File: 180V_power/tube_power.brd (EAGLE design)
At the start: 50 x 50 mm, 25 parts, among them IC1 NE555D, Q1 IRF740S, Q2 BC546

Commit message: new stuff
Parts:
- removed 7805: 78, iStivi - Transistor-FET-reg:SO08
- removed Q2: BC546, iStivi - Transistor-FET-reg:TO92-EBC
- removed U$1, U$2: (no value), iStivi - Board-Holes:3,2
- removed VR1: 1K, iStivi - RCLD:CA6V
- added R7: 1K, iStivi - RCLD:CA6V
- added U$5, U$6: (no value), iStivi - Board-Holes:3,0
- added U1: TLV1117-5SOT-223, iStivi - Transistor-FET-reg:SOT-223
- added U2: BC817, iStivi - Transistor-FET-reg:SOT-23
- L1: device iStivi - RCLD:TFI0307 -> iStivi - RCLD:RBL0712
- Q1: device iStivi - Transistor-FET:TO263 -> iStivi - Transistor-FET-reg:TO263
- R1: value 56K -> 220K; device iStivi - RCLD:R1206 -> iStivi - RCLD:0207/10
- R2: value 10K -> 470R; device iStivi - RCLD:R1206 -> iStivi - RCLD:0207/10
- R4: value 470R -> 10K; device iStivi - RCLD:0207/10 -> iStivi - RCLD:R1206
- R5: value 220K -> 56K; device iStivi - RCLD:0207/10 -> iStivi - RCLD:R1206
- U$3, U$4: device iStivi - Board-Holes:3,2 -> iStivi - Board-Holes:3,0
- moved C1 33.1 mm to (43.2, 15.2), turned to 0 degrees
- moved R4 26.2 mm to (20.3, 27.9), turned to 180 degrees
- moved Q1 25.4 mm to (34.3, 29.2)
- moved VIN 24.4 mm to (47.0, 24.1), turned to 90 degrees
- moved R5 22.3 mm to (20.3, 22.9), turned to 180 degrees
- moved L1 19.0 mm to (5.08, 14.6), turned to 90 degrees
- moved D1 17.9 mm to (12.7, 13.3), turned to 270 degrees
- moved C4 17.2 mm to (21.0, 12.1), turned to 0 degrees
- moved 180V 16.6 mm to (14.0, 2.54)
- moved C5 16.2 mm to (33.0, 5.71), turned to 0 degrees
- moved IC1 16.2 mm to (21.6, 33.7)
- moved R3 14.5 mm to (20.3, 25.4), turned to 180 degrees
- moved R6 14.5 mm to (20.3, 20.3), turned to 180 degrees
- moved R2 10.6 mm to (15.2, 31.1), turned to 90 degrees
- moved U$4 10.0 mm to (5.00, 35.0)
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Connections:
- net 180V: now also R1.2; no longer R5.2
- net 5V: now also U1.2, U1.4; no longer 7805.2, 7805.3, 7805.6, 7805.7
- net GND: now also R2.1, U1.1, U2.2; no longer 7805.1, Q2.E, R4.1
- net N$10: now also R7.S, U2.1; no longer Q2.B, VR1.S
- net N$26: now also L1.P$2, R5.2, U1.3; no longer 7805.4, L1.2, R1.2
- net N$3: now also R5.1, U2.3; no longer Q2.C, R1.1
- net N$4: now also R4.2; no longer R2.2
- net N$5: now also R4.1; no longer R2.1
- net N$6: now also L1.P$1; no longer L1.1
- net N$8: now also R1.1, R7.E; no longer R5.1, VR1.E
- net N$9: now also R2.2, R7.A; no longer R4.2, VR1.A
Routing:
- net N$1: track 40.9 -> 15.3 mm, vias 2 -> 0
- net GND: track 136.1 -> 113.0 mm
- net N$10: track 33.7 -> 10.9 mm, vias 0 -> 1
- net N$6: track 50.4 -> 69.8 mm, vias 2 -> 1
- net 180V: track 25.2 -> 42.5 mm
- net N$4: track 35.9 -> 18.9 mm
- net N$26: track 116.6 -> 104.3 mm, vias 0 -> 2
- net 5V: track 36.9 -> 24.9 mm, vias 1 -> 0
- net N$5: track 30.9 -> 22.0 mm, vias 4 -> 2
- net N$8: track 4.60 -> 11.1 mm
- net N$3: track 27.7 -> 31.7 mm, vias 1 -> 3
- net N$2: track 7.80 -> 3.81 mm
- net N$9: track 16.6 -> 12.7 mm
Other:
- board size 50 x 50 mm -> 50 x 40 mm
- board text removed: "100uH"
- board text removed: "10uF"
- board text removed: "180V"
- board text removed: "1K"
- board text removed: "2.2uF"
- board text removed: "220K"
- board text removed: "330uF"
- board text removed: "470R"
- board text removed: "5V"
- board text removed: "5V/180V POWER BOARD"
- board text removed: "7805"
- board text removed: "9-12V"
- board text removed: "BC546"
- board text removed: "GND"
- board text removed: "IRF740"
- board text removed: "NE555"
- board text removed: "POWER BOARD"
- board text removed: "Vin"
- board text removed: "iStivi"

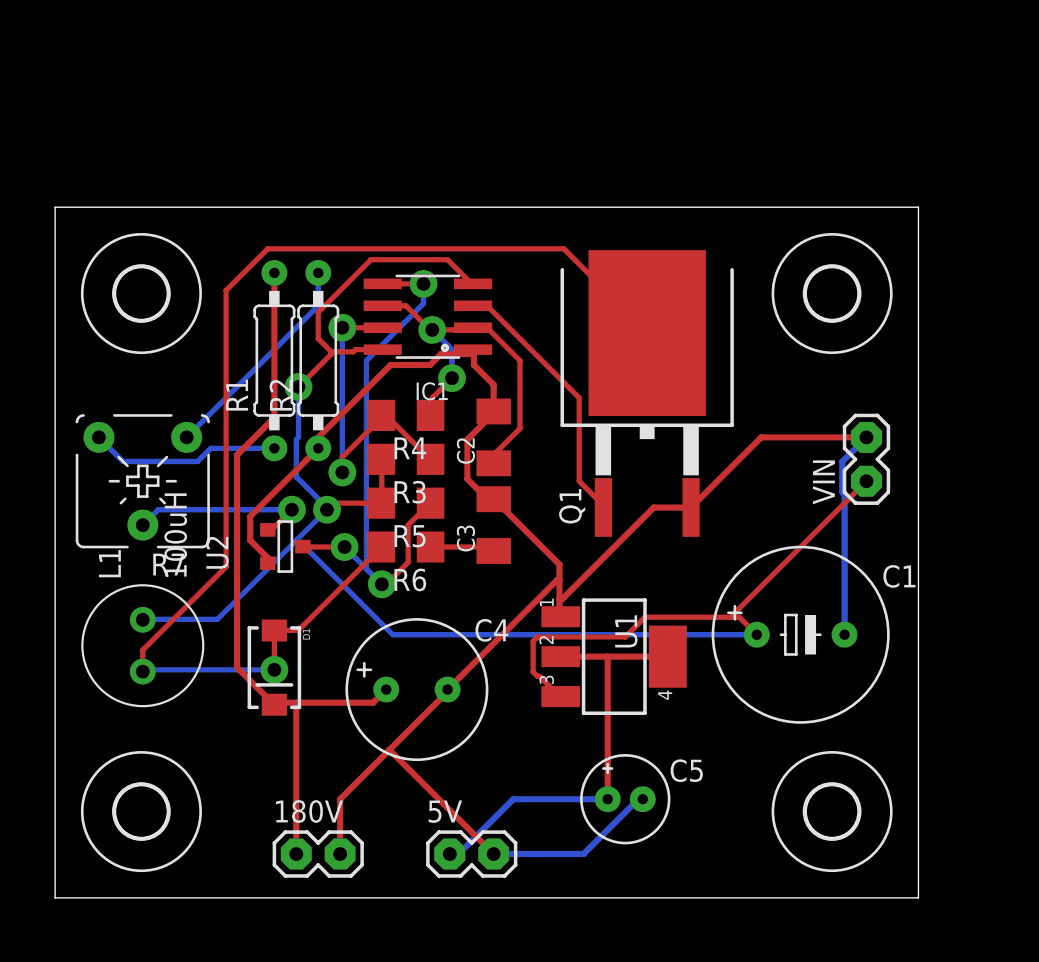
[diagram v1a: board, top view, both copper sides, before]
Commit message: made board smaller for production
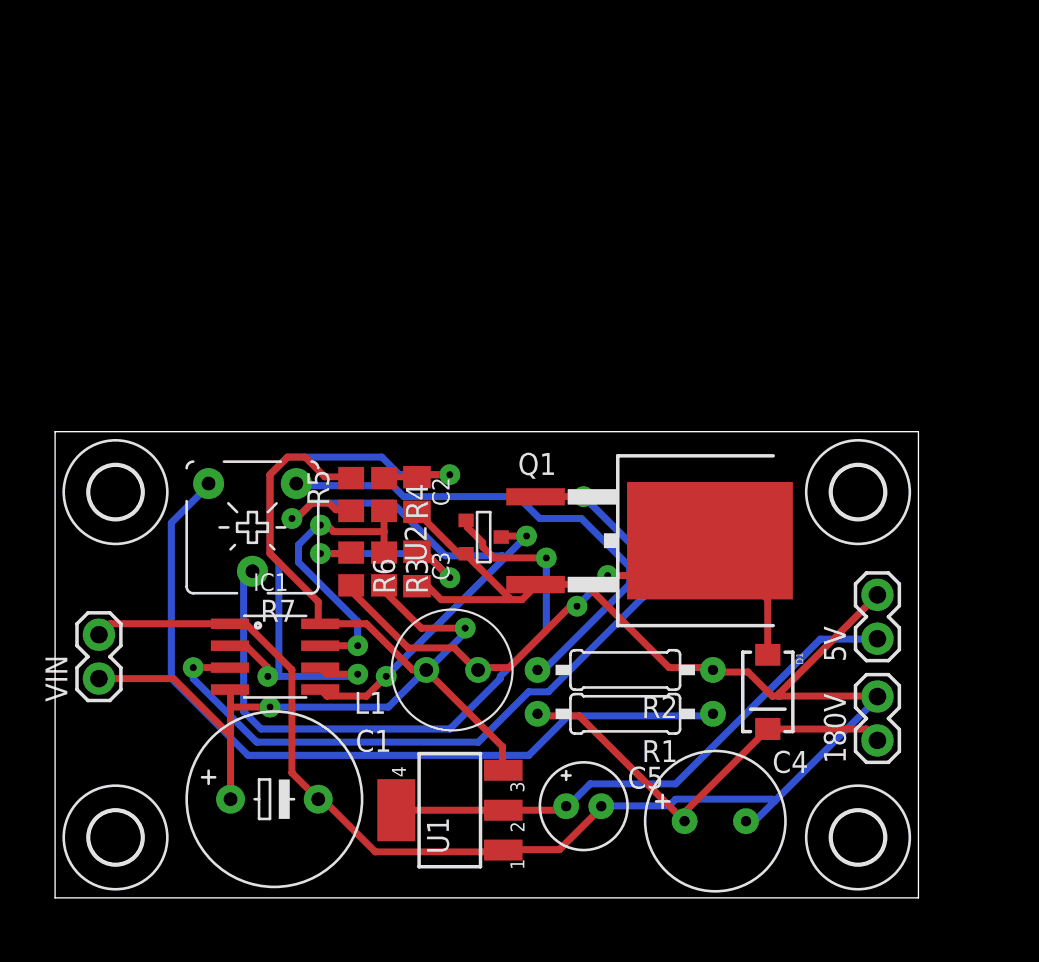
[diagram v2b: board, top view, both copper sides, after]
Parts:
- removed U$3, U$6: (no value), iStivi - Board-Holes:3,0
- added U$1, U$2: (no value), iStivi - Board-Holes:3,0-SMALL
- C2, C3: device iStivi - RCLD:C1206K -> iStivi - RCLD:C0805K
- R3, R4, R5, R6: device iStivi - RCLD:R1206 -> iStivi - RCLD:R0805
- U$4, U$5: device iStivi - Board-Holes:3,0 -> iStivi - Board-Holes:3,0-SMALL
- moved U$4 52.1 mm to (46.5, 3.50)
- moved VIN 45.9 mm to (2.54, 12.7)
- moved 180V 34.3 mm to (47.6, 9.12), turned to 90 degrees
- moved C1 31.9 mm to (12.7, 5.71)
- moved R1 28.8 mm to (33.0, 10.7), turned to 180 degrees
- moved D1 28.6 mm to (41.3, 11.9)
- moved 5V 27.7 mm to (47.6, 15.0), turned to 90 degrees
- moved R2 25.2 mm to (33.0, 13.2), turned to 180 degrees
- moved IC1 21.6 mm to (12.7, 14.0), turned to 270 degrees
- moved C4 18.9 mm to (38.2, 4.45)
- moved L1 18.0 mm to (23.0, 13.2), turned to 180 degrees
- moved U1 13.0 mm to (22.9, 5.08), turned to 90 degrees
- moved U$5 11.6 mm to (46.5, 23.5)
- moved U2 11.5 mm to (24.8, 20.9)
- moved Q1 8.53 mm to (34.4, 20.7), turned to 270 degrees
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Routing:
- net N$26: track 104.3 -> 67.3 mm
- net N$8: track 11.1 -> 46.5 mm
- net N$6: track 69.8 -> 37.6 mm, vias 1 -> 2
- net N$1: track 15.3 -> 43.8 mm, vias 0 -> 2
- net N$10: track 10.9 -> 38.8 mm
- net 180V: track 42.5 -> 25.2 mm
- net N$9: track 12.7 -> 29.8 mm
- net N$5: track 22.0 -> 37.9 mm, vias 2 -> 3
- net N$2: track 3.81 -> 12.5 mm, vias 0 -> 2
- net 5V: track 24.9 -> 32.0 mm
- net GND: track 113.0 -> 106.3 mm
- net N$3: track 31.7 -> 35.5 mm
- net N$4: track 18.9 -> 17.4 mm
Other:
- board size 50 x 40 mm -> 50 x 27 mm

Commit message: board almost final
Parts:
- moved D1 0.63 mm to (41.3, 12.6)
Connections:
- net N$1 renamed OUT
- net N$10 renamed VAR
- net N$2 renamed R6
- net N$26 renamed VCC
- net N$3 renamed CON
- net N$4 renamed DIS
- net N$5 renamed THR
- net N$6 renamed L1
- net N$8 renamed R1
- net N$9 renamed R2
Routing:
- net 180V: track 25.2 -> 26.4 mm
- net OUT: track 43.8 -> 44.9 mm
- net GND: track 106.3 -> 107.0 mm
- net L1: track 37.6 -> 36.9 mm
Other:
- board text added: "100uH"
- board text added: "10uF"
- board text added: "180V"
- board text added: "2.2uF"
- board text added: "220K"
- board text added: "330uF"
- board text added: "470R"
- board text added: "5V"
- board text added: "D1"
- board text added: "GND"
- board text added: "IRF740"
- board text added: "L1"
- board text added: "NE555"
- board text added: "TLV1117"
- board text added: "VIN"
- board text added: "VR1"

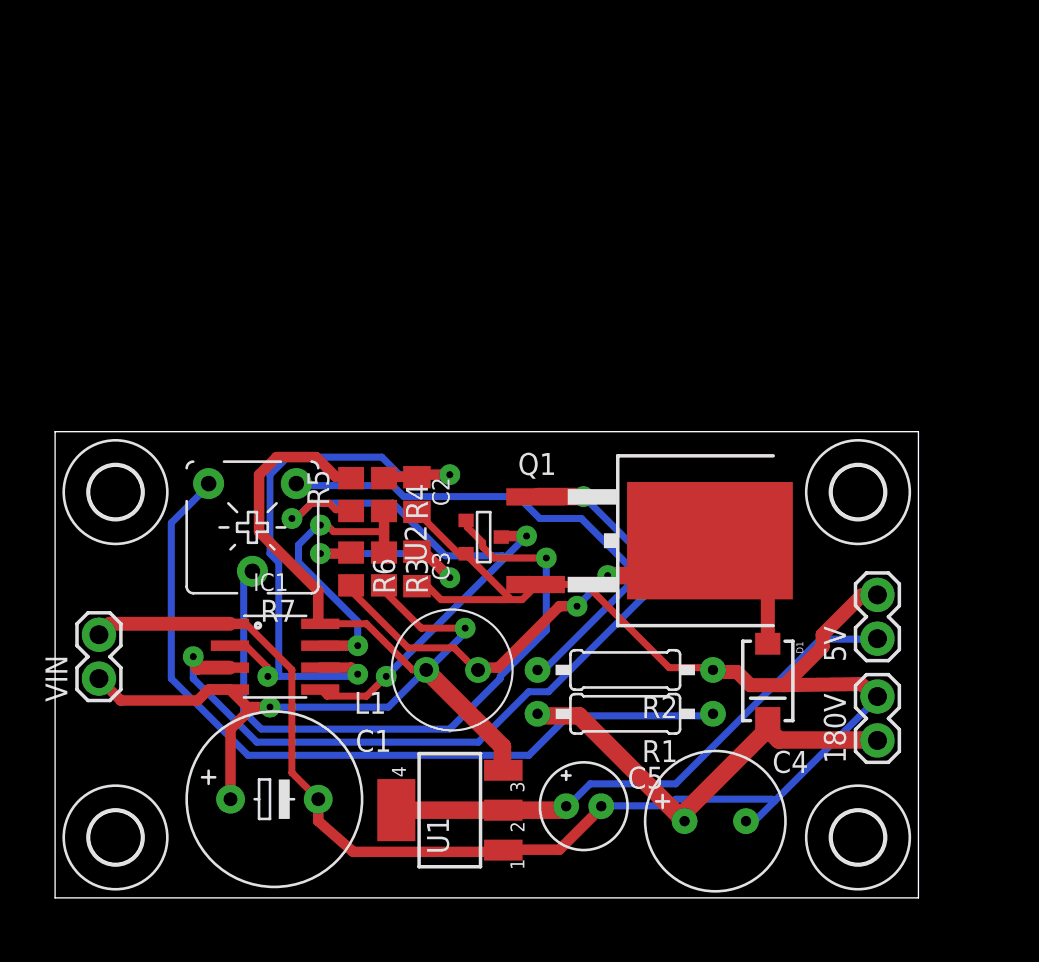
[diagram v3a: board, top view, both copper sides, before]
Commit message: added protection diode
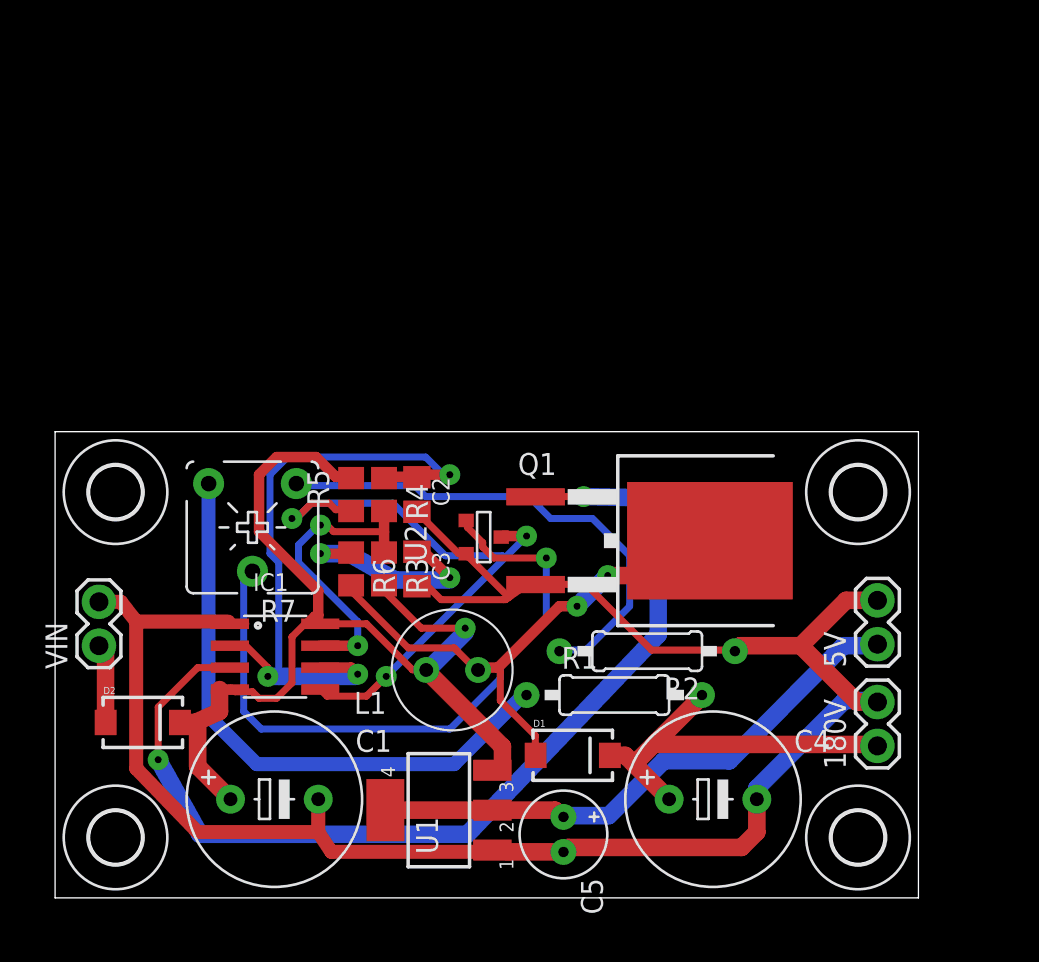
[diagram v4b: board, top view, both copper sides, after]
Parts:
- added D2: (no value), iStivi - RCLD:SMA-DIODE
- C4: device iStivi - RCLD:E3,5-8 -> iStivi - RCLD:E5-10,5
- moved D1 12.1 mm to (30.0, 8.26), turned to 0 degrees
- moved C5 2.01 mm to (29.4, 3.67), turned to 270 degrees
- moved VIN 1.91 mm to (2.54, 14.6)
- moved R2 1.67 mm to (34.3, 14.3)
- moved C4 1.28 mm to (38.1, 5.71)
- moved R1 1.26 mm to (32.4, 11.7), turned to 0 degrees
- moved U1 0.63 mm to (22.2, 5.08)
- moved 180V 0.32 mm to (47.6, 8.80)
- moved 5V 0.32 mm to (47.6, 14.7)
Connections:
- new net N$1: D2.A, VIN.1
- net VCC: now also D2.C; no longer VIN.1
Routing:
- net OUT: track 44.9 -> 58.8 mm
- net R1: track 46.5 -> 34.7 mm
- net VCC: track 67.6 -> 59.6 mm, vias 2 -> 1
- net GND: track 107.0 -> 114.2 mm
- net N$1: track 0.00 -> 4.61 mm
- net 180V: track 26.4 -> 23.1 mm
- net L1: track 36.9 -> 35.6 mm
- net 5V: track 32.0 -> 32.8 mm
- net R2: track 29.8 -> 29.2 mm
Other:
- board text added: "9-12V"
- board text added: "C4"
- board text added: "R1"
- board text added: "R2"
- board text removed: "2.2uF"
- board text removed: "220K"
- board text removed: "470R"
- board text removed: "D1"
- board text removed: "NE555"

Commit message: lalala
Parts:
- moved R1 3.88 mm to (35.6, 14.0)
- moved L1 3.15 mm to (25.4, 15.2)
- moved R2 2.56 mm to (35.6, 16.5)
- moved U$1 2.55 mm to (4.00, 26.0)
- moved U$5 2.55 mm to (46.0, 26.0)
- moved Q1 2.18 mm to (34.3, 22.9)
- moved U2 2.00 mm to (24.8, 22.9)
- moved D1 1.80 mm to (28.7, 9.53)
- moved C5 1.51 mm to (27.9, 3.81)
- moved C4 1.42 mm to (36.8, 6.35)
- moved U1 1.42 mm to (21.6, 6.35), turned to 180 degrees
- moved R7 1.41 mm to (11.4, 22.9)
- moved C2 1.00 mm to (21.0, 24.4)
- moved C3 1.00 mm to (21.0, 20.1)
- moved R3 1.00 mm to (19.1, 20.1)
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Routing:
- net THR: track 38.0 -> 64.0 mm, vias 3 -> 2
- net VCC: track 59.6 -> 74.5 mm
- net R1: track 34.7 -> 46.6 mm
- net OUT: track 58.8 -> 63.4 mm
- net CON: track 35.5 -> 31.2 mm
- net R2: track 29.2 -> 25.2 mm
- net 5V: track 32.8 -> 36.7 mm
- net DIS: track 17.4 -> 15.5 mm, vias 2 -> 0
- net VAR: track 38.8 -> 37.2 mm
- net L1: track 35.6 -> 34.3 mm, vias 2 -> 3
- net GND: track 114.2 -> 115.2 mm
- net N$1: track 4.61 -> 5.28 mm
- net R6: track 12.5 -> 11.8 mm
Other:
- board size 50 x 27 mm -> 50 x 30 mm
- board text added: "B"
- board text added: "NIXIE POWER SUPPLY"
- board text added: "oy"
- board text added: "uzz"

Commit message: new format
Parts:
- added U$3: (no value), iStivi - Logos:BUZZBOY-SILK
- added U$6: (no value), iStivi - Logos:BUZZBOY
- 180V, 5V, VIN: device iStivi - Header-Connector:1X02 -> iStivi - Header-Connector:SCREWTERMINAL-3.5MM-2
- moved U$4 3.89 mm to (49.9, 4.00)
- moved U$5 3.89 mm to (49.9, 26.0)
- moved VIN 3.56 mm to (6.09, 15.1)
- moved C1 2.46 mm to (15.2, 6.35)
- moved C2 2.46 mm to (23.4, 24.4)
- moved C3 2.46 mm to (23.4, 20.1)
- moved C4 2.46 mm to (39.3, 6.35)
- moved D1 2.46 mm to (31.2, 9.53)
- moved IC1 2.46 mm to (15.2, 14.6)
- moved L1 2.46 mm to (27.9, 15.2)
- moved Q1 2.46 mm to (36.8, 22.9)
- moved R1 2.46 mm to (38.0, 14.0)
- moved R2 2.46 mm to (38.0, 16.5)
- moved R3 2.46 mm to (21.5, 20.1)
- moved R4 2.46 mm to (21.5, 24.4)
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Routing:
- net VCC: track 74.5 -> 77.0 mm
- net N$1: track 5.28 -> 7.57 mm
- net GND: track 115.2 -> 113.8 mm
- net 180V: track 23.5 -> 22.5 mm
- net 5V: track 36.7 -> 37.5 mm
- net THR: track 64.0 -> 64.6 mm
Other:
- board size 50 x 30 mm -> 55 x 30 mm
- board text removed: "100uH"
- board text removed: "B"
- board text removed: "oy"
- board text removed: "uzz"
